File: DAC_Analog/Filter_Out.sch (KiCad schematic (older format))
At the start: 22 parts

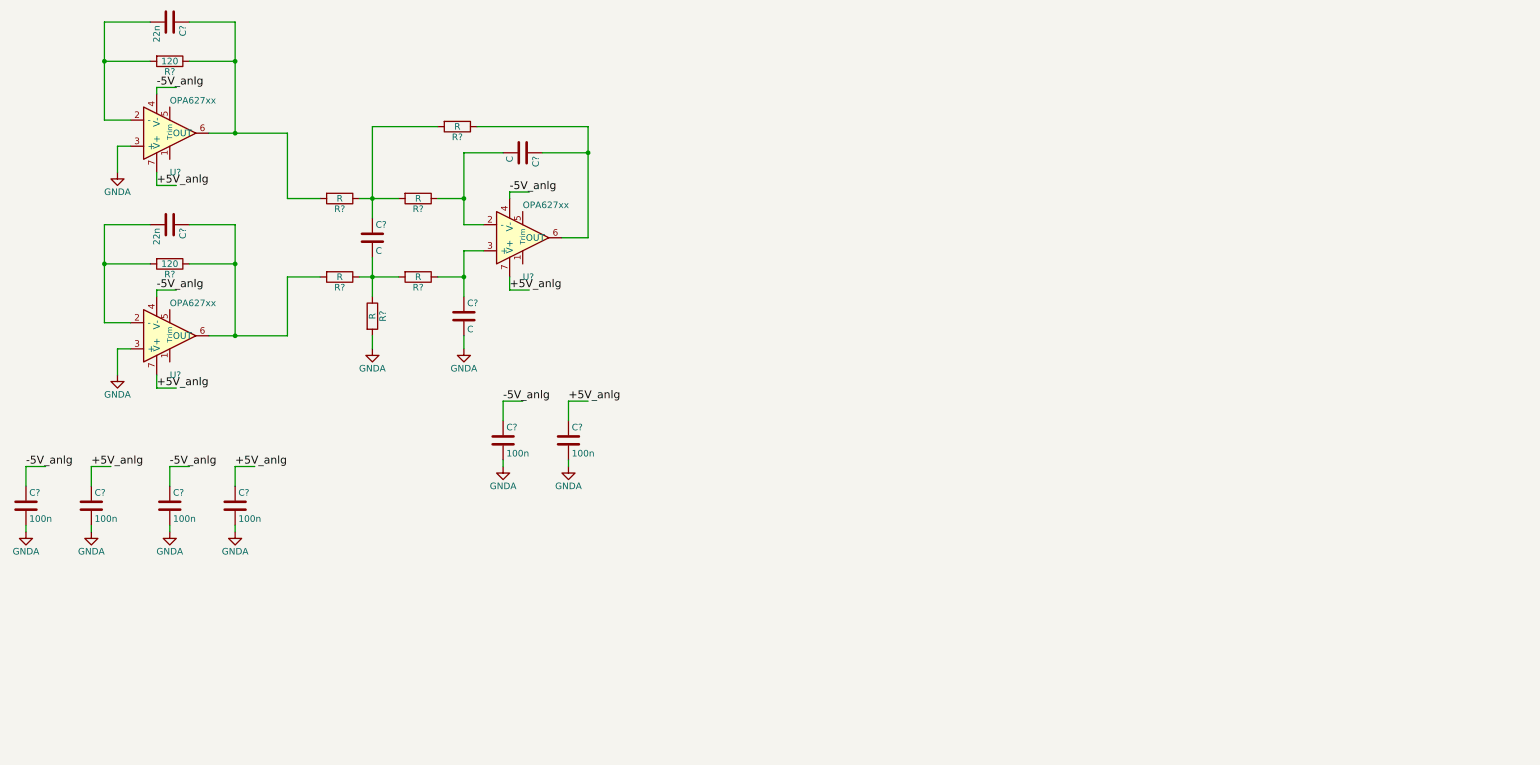
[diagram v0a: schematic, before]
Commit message: design analog output
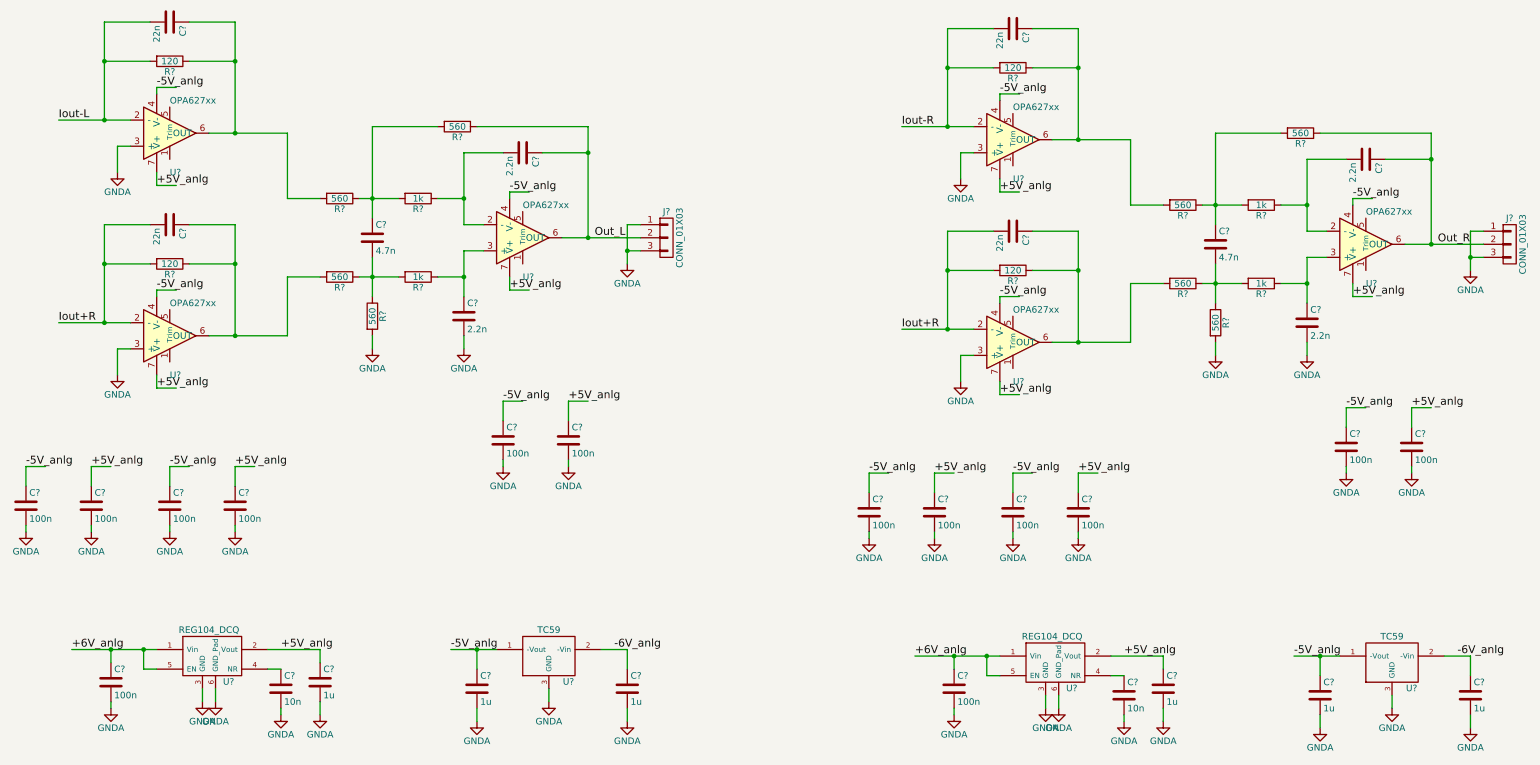
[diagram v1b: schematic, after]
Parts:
- added C? (x8): 100n, symbol C
- added C? (x2): 10n, symbol C
- added C? (x6): 1u, symbol C
- added C? (x2): 22n, symbol C
- added C?: 4.7n, symbol C
- added C? (x2): 2.2n, symbol C
- added J? (x2): CONN_01X03, symbol CONN_01X03
- added R? (x2): 120, symbol R
- added R? (x4): 560, symbol R
- added R? (x2): 1k, symbol R
- added U? (x2): REG104_DCQ, symbol REG104_DCQ
- added U? (x2): TC59, symbol TC59
- added U? (x3): OPA627xx, symbol OPA627xx
- C?: value C -> 4.7n
- C? (x2): value C -> 2.2n
- R? (x4): value R -> 560
- R? (x2): value R -> 1k
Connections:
- net labels added: +6V_anlg, -6V_anlg, Iout+R, Iout-L, Iout-R, Out_L, Out_R
- wire segments 72 -> 188
